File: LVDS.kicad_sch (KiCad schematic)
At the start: 1 part, among them J3 QSH-030-01-X-D-A-XX

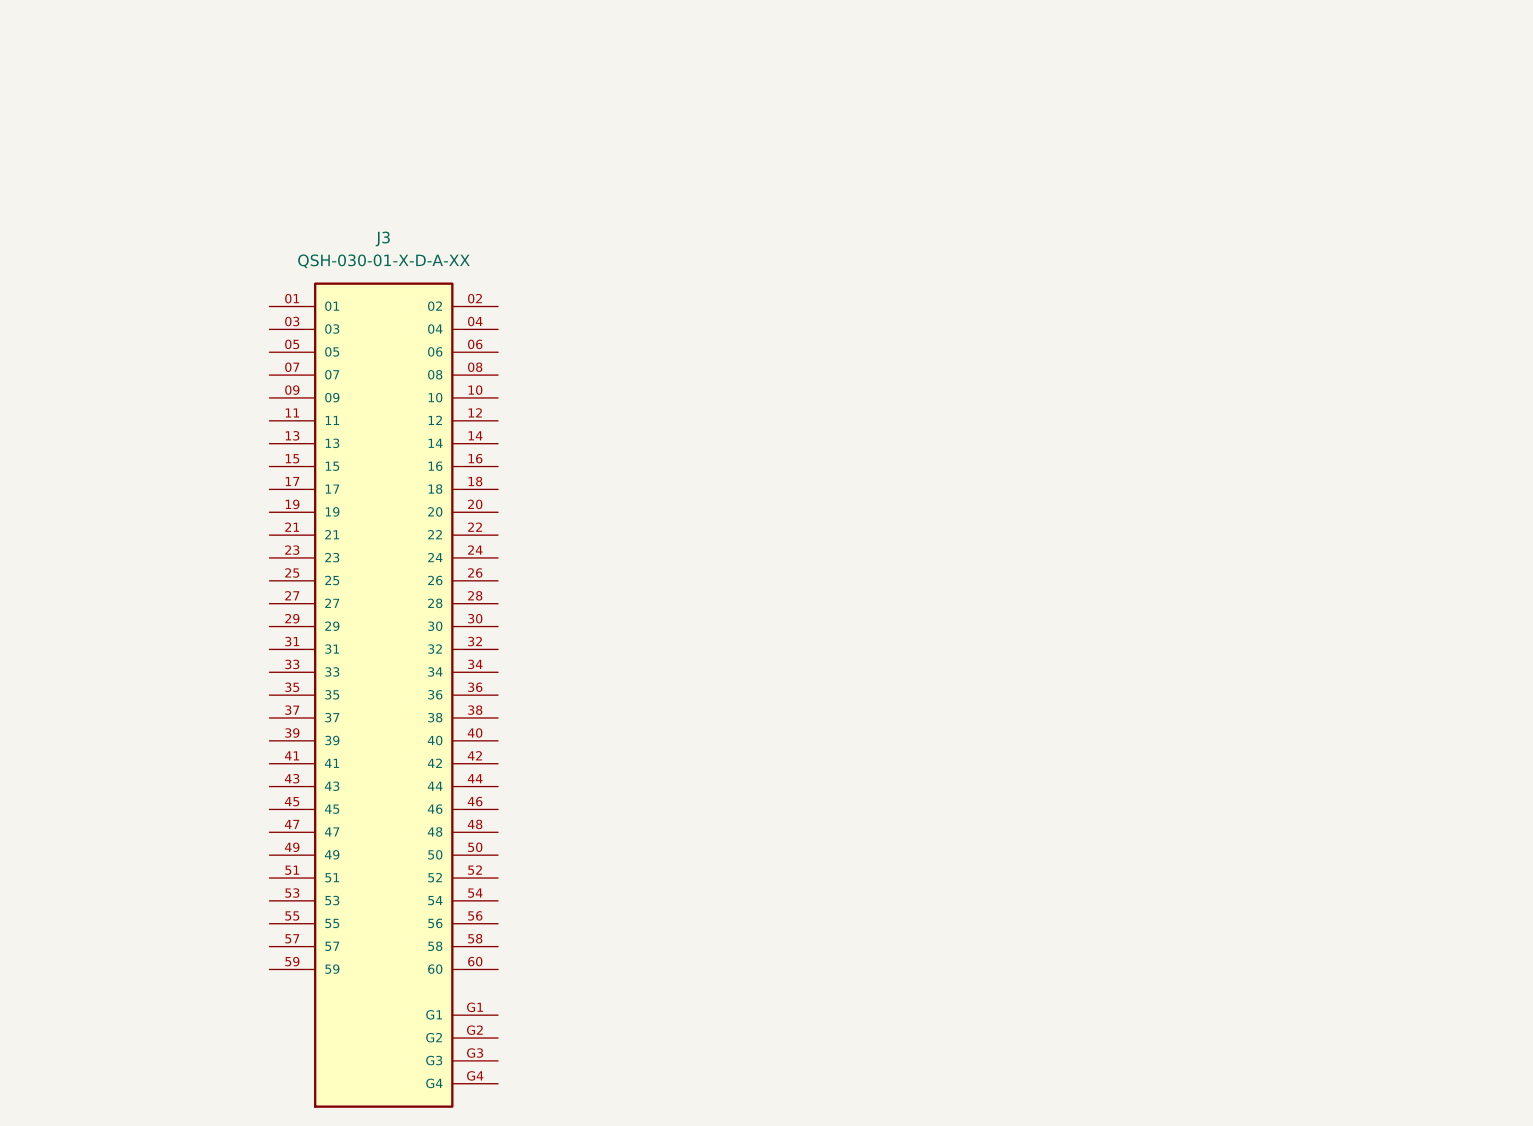
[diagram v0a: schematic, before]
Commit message: Replaced LVDS connector with correct one and started pinning it out
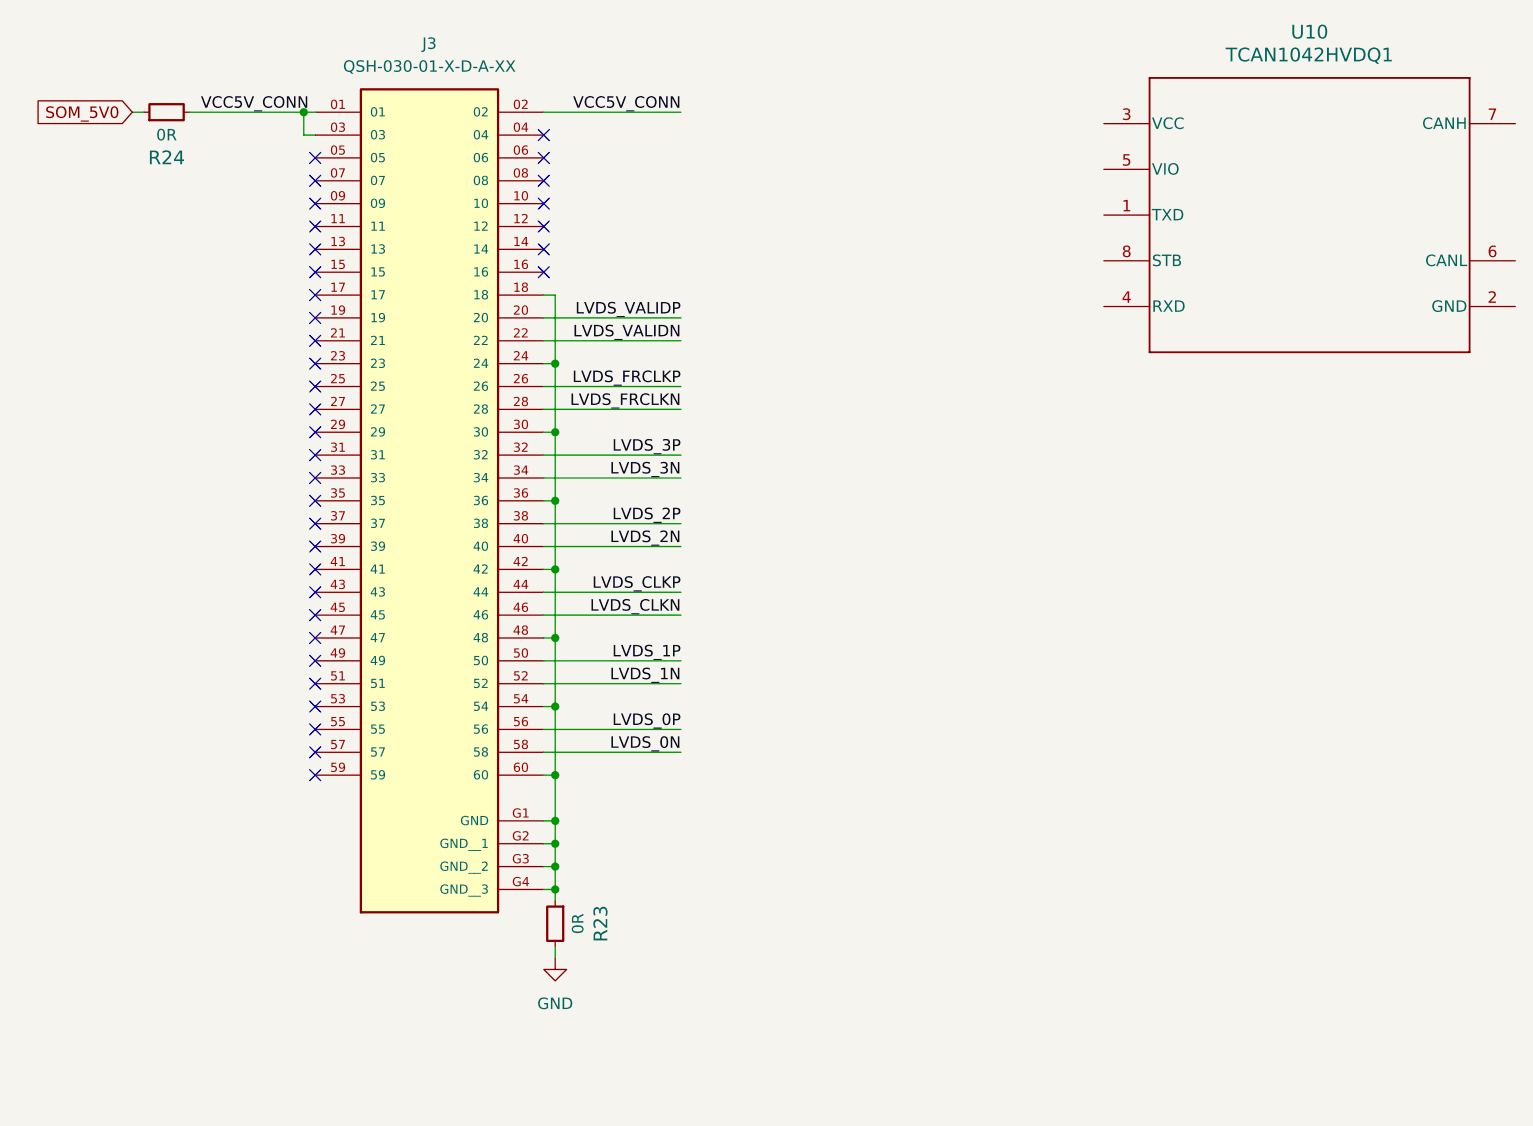
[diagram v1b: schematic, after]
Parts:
- added R23, R24: R_0R_0402, kria-k26-devboard-footprints:R_0402_1005Metric, symbol kria-k26-devboard:R_0R_0402
- added U10: TCAN1042HVDQ1, kria-k26-devboard-footprints:D0008A_L, symbol kria-k26-devboard:TCAN1042HVDQ1
- J3: footprint kria-k26-devboard-footprints:SAMTEC_QSH-030-01-X-D-A-XX -> kria-k26-devboard-footprints:SAMTEC-QTH-030-01-X-D-A; symbol kria-k26-devboard:QSH-030-01-X-D-A-XX -> kria-k26-devboard:QTH-030-01-X-D-A; MAXIMUM_PACKAGE_HEIGHT 3.05 mm -> 4.347mm; PARTREV M -> L
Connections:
- net VCC5V_CONN: now reaches J3.01
- net VCC5V_CONN: now also J3.02, J3.03, R24.2
- net at J3.18: now also J3.24, J3.30, J3.36, J3.42, J3.48, J3.54, J3.60, J3.G1 (GND), J3.G2 (GND__1), J3.G3 (GND__2), J3.G4 (GND__3), R23.1
- net LVDS_VALIDP: now reaches J3.20
- net LVDS_VALIDN: now reaches J3.22
- net LVDS_FRCLKP: now reaches J3.26
- net LVDS_FRCLKN: now reaches J3.28
- net LVDS_3P: now reaches J3.32
- net LVDS_3N: now reaches J3.34
- net LVDS_2P: now reaches J3.38
- net LVDS_2N: now reaches J3.40
- net LVDS_CLKP: now reaches J3.44
- net LVDS_CLKN: now reaches J3.46
- net LVDS_1P: now reaches J3.50
- net LVDS_1N: now reaches J3.52
- net LVDS_0P: now reaches J3.56
- net LVDS_0N: now reaches J3.58
- new net GND: R23.2
- new net SOM_5V0: R24.1
- no-connect marks 0 -> 35
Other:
- moved on the sheet: J3

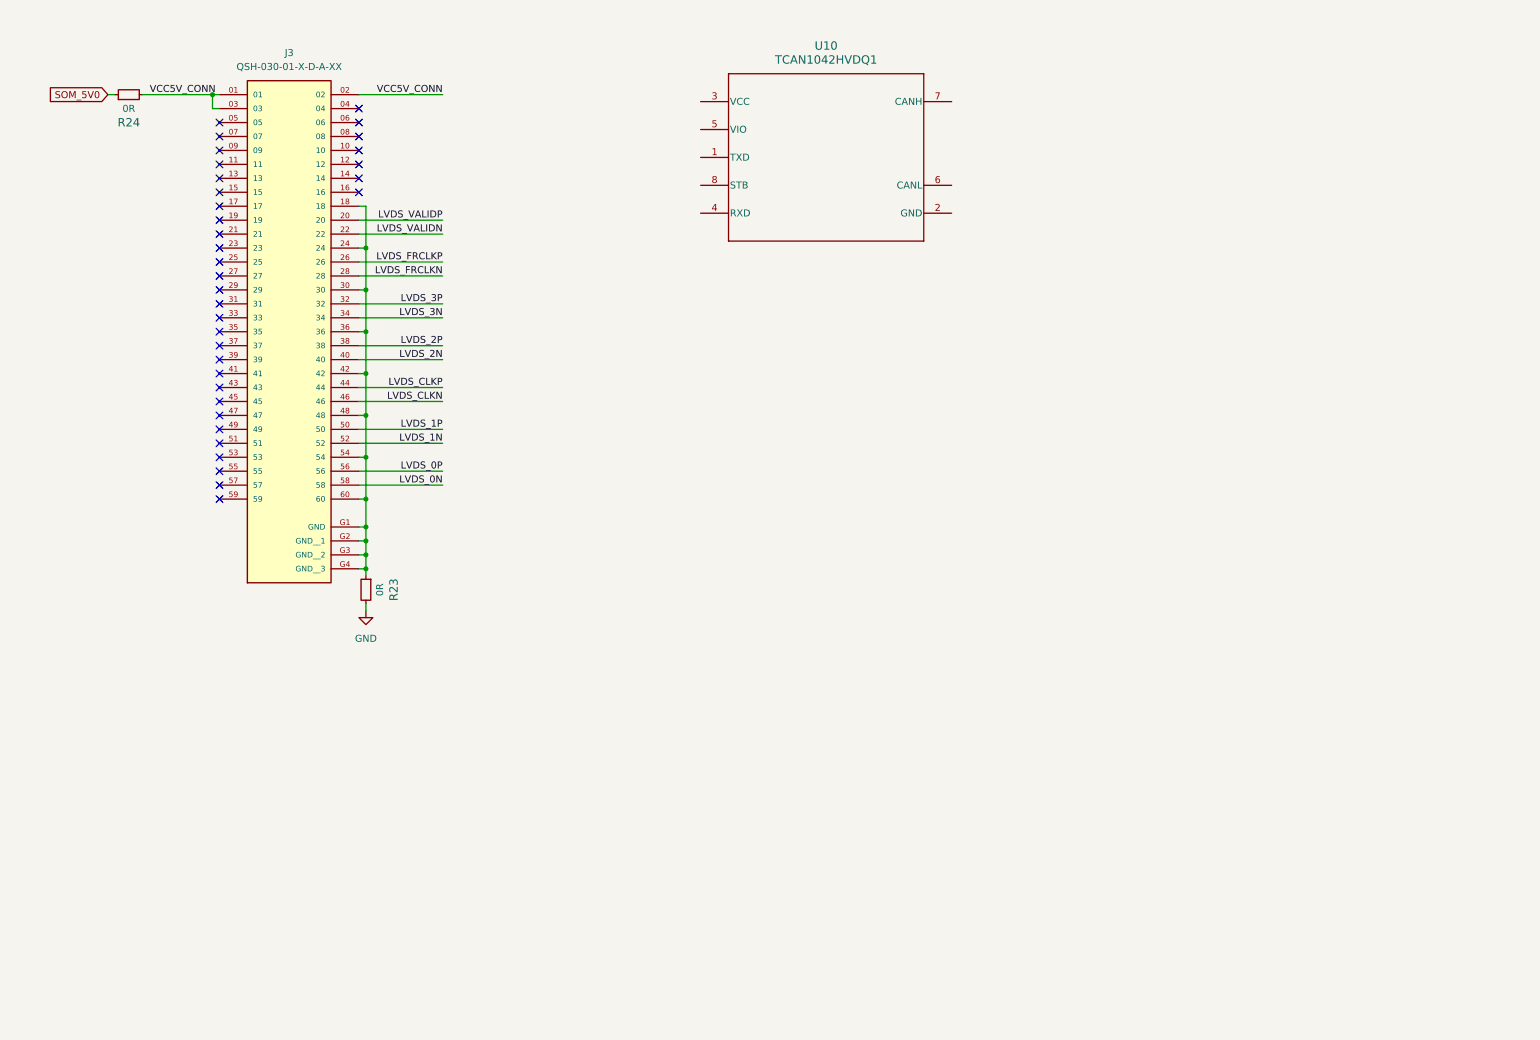
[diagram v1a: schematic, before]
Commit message: Added all components and finished first attempt at schematic
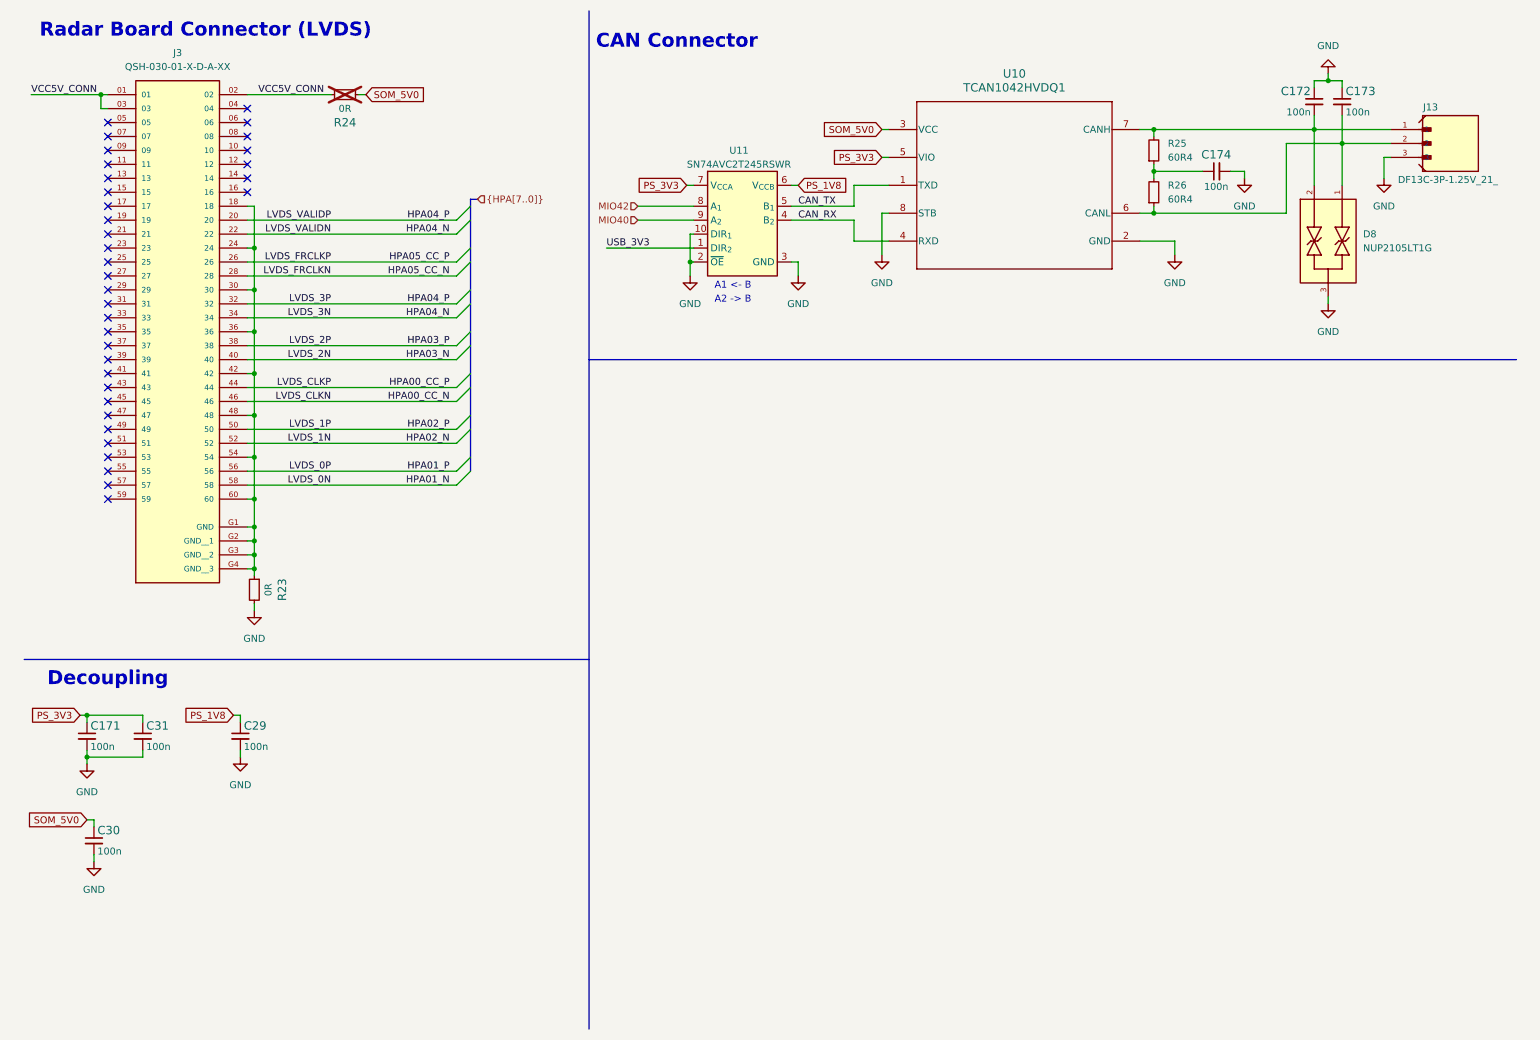
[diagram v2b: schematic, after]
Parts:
- added C171, C172, C173, C174, C29, C30, C31: C_100n_0402, kria-k26-devboard-footprints:C_0402_1005Metric, symbol kria-k26-devboard:C_100n_0402
- added D8: NUP2105LT1G, kria-k26-devboard-footprints:SOT95P237X111-3N, symbol kria-k26-devboard:NUP2105LT1G
- added J13: DF13C-3P-1.25V_21_, kria-k26-devboard-footprints:HRS_DF13C-3P-1.25V_21_, symbol kria-k26-devboard:DF13C-3P-1.25V_21_
- added R25, R26: R_60R4_0402, kria-k26-devboard-footprints:R_0402_1005Metric, symbol kria-k26-devboard:R_60R4_0402
- added U11: SN74AVC2T245_UQFN, kria-k26-devboard-footprints:UQFN-10_1.4x1.8x0.5mm_P0.4mm, symbol kria-k26-devboard:SN74AVC2T245_UQFN
- R24: now not fitted; now left out of the parts list
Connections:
- net LVDS_VALIDN is gone; now on net HPA04_N: J3.22
- net LVDS_VALIDP is gone; now on net HPA04_P: J3.20
- net GND: now also U10.2 (GND), U10.8 (STB), C171.2, C172.1, C173.1, C174.2, C29.2, C30.2, C31.2, D8.3, J13.3, U11.10 (DIR_{1}), U11.2 (~{OE}), U11.3 (GND)
- net SOM_5V0: now also R24.2, U10.3 (VCC), C30.1; no longer R24.1
- net VCC5V_CONN: now also R24.1; no longer R24.2
- net CAN_TX: now reaches U10.1 (TXD)
- net CAN_TX: now also U11.5 (B_{1})
- net CAN_RX: now reaches U10.4 (RXD)
- net CAN_RX: now also U11.4 (B_{2})
- net PS_3V3: now reaches U10.5 (VIO)
- net PS_3V3: now also C171.1, C31.1, U11.7 (V_{CCA})
- net at U10.6 (CANL): now also C173.2, D8.1, J13.2, R26.1
- net at U10.7 (CANH): now also C172.2, D8.2, J13.1, R25.2
- net LVDS_0N renamed HPA01_N
- net LVDS_0P renamed HPA01_P
- net LVDS_1N renamed HPA02_N
- net LVDS_1P renamed HPA02_P
- net LVDS_2N renamed HPA03_N
- net LVDS_2P renamed HPA03_P
- net LVDS_3N renamed HPA04_N
- net LVDS_3P renamed HPA04_P
- net LVDS_CLKN renamed HPA00_CC_N
- net LVDS_CLKP renamed HPA00_CC_P
- net LVDS_FRCLKN renamed HPA05_CC_N
- net LVDS_FRCLKP renamed HPA05_CC_P
- new net: C174.1, R25.1, R26.2
- new net MIO40: U11.9 (A_{2})
- new net MIO42: U11.8 (A_{1})
- new net PS_1V8: C29.1, U11.6 (V_{CCB})
- new net USB_3V3: U11.1 (DIR_{2})
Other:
- note added: "A1 <- B"
- note added: "A2 -> B"
- note added: "CAN Connector"
- note added: "Decoupling"
- note added: "Radar Board Connector (LVDS)"
- moved on the sheet: J3, R23, U10
